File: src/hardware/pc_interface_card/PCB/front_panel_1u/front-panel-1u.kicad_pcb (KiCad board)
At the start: 2 copper layers, 25 x 100 mm, 5 parts

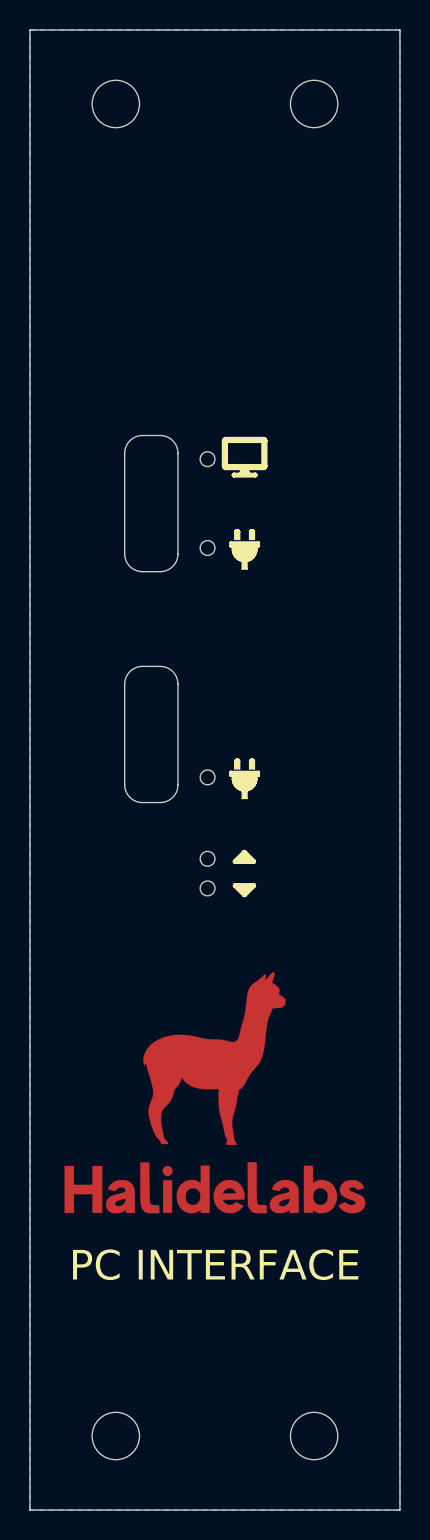
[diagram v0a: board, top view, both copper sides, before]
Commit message: adding barrel jack connector for powering PC interface card and mooving the status LEDs on the front panel
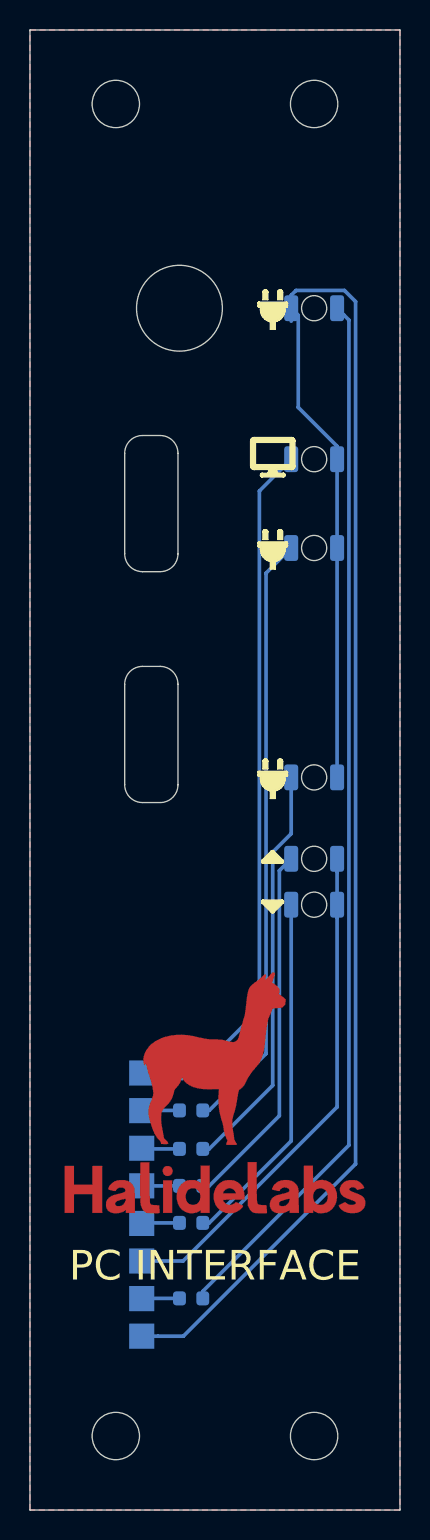
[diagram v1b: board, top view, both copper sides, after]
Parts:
- added D1: LED, LED_SMD:LED_1206_3216Metric_ReverseMount_Hole1.8x2.4mm, B.Cu at (149.2, 105.0)
- added D2: LED, LED_SMD:LED_1206_3216Metric_ReverseMount_Hole1.8x2.4mm, B.Cu at (149.2, 108.1)
- added D3: LED, LED_SMD:LED_1206_3216Metric_ReverseMount_Hole1.8x2.4mm, B.Cu at (149.2, 78.0)
- added D4: LED, LED_SMD:LED_1206_3216Metric_ReverseMount_Hole1.8x2.4mm, B.Cu at (149.2, 84.0)
- added D5: LED, LED_SMD:LED_1206_3216Metric_ReverseMount_Hole1.8x2.4mm, B.Cu at (149.2, 99.5)
- added D6: LED, LED_SMD:LED_1206_3216Metric_ReverseMount_Hole1.8x2.4mm, B.Cu at (149.2, 67.8)
- added J1: Conn_01x08, Connector_PinHeader_2.54mm:PinHeader_1x08_P2.54mm_Vertical, B.Cu at (137.6, 119.5)
- added R1: R, Resistor_SMD:R_0603_1608Metric, B.Cu at (140.9, 127.1)
- added R2: R, Resistor_SMD:R_0603_1608Metric, B.Cu at (140.9, 129.6)
- added R3: R, Resistor_SMD:R_0603_1608Metric, B.Cu at (140.9, 119.5)
- added R4: R, Resistor_SMD:R_0603_1608Metric, B.Cu at (140.9, 122.0)
- added R5: R, Resistor_SMD:R_0603_1608Metric, B.Cu at (140.9, 124.6)
- added R6: R, Resistor_SMD:R_0603_1608Metric, B.Cu at (140.9, 134.7)
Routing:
- net GND: track 0.00 -> 117.1 mm
- net Net-(D6-Pad2): track 0.00 -> 71.3 mm
- net Net-(D3-Pad2): track 0.00 -> 44.0 mm
- net Net-(D4-Pad2): track 0.00 -> 40.7 mm
- net /FT_PB_5V: track 0.00 -> 34.3 mm
- net Net-(D5-Pad2): track 0.00 -> 27.8 mm
- net Net-(D1-Pad1): track 0.00 -> 24.8 mm
- net Net-(D2-Pad1): track 0.00 -> 24.2 mm
- net /USB_B_PWR_OK: track 0.00 -> 2.57 mm
- net /FT_RXLED: track 0.00 -> 2.56 mm
- net /USBC_IO_PWR_CONN_VBUS: track 0.00 -> 2.56 mm
- net /JACK_PWR_OK: track 0.00 -> 2.56 mm
- net /USB_A_PWR_OK: track 0.00 -> 2.56 mm
- net /FT_TXLED: track 0.00 -> 2.55 mm
- added copper zone on F.Cu, net (none)
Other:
- outline, holes or cut-outs redrawn
